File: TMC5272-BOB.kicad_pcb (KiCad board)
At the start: 2 copper layers, 103.1 x 51.1 mm, 23 parts, among them J1 Conn_02x14, J10 Conn_01x04_Socket, J11 Conn_01x04_Socket, J2 Conn_02x14, J22 Conn_01x01_Pin, J24 Conn_01x02_Socket, J26 Conn_01x01_Pin, J3 Conn_02x16, J4 Conn_02x12, J5 Conn_01x02_Pin, J6 Conn_01x03_Pin, J7 Conn_01x02_Pin, J8 Conn_01x02_Pin, J9 Conn_01x01_Pin

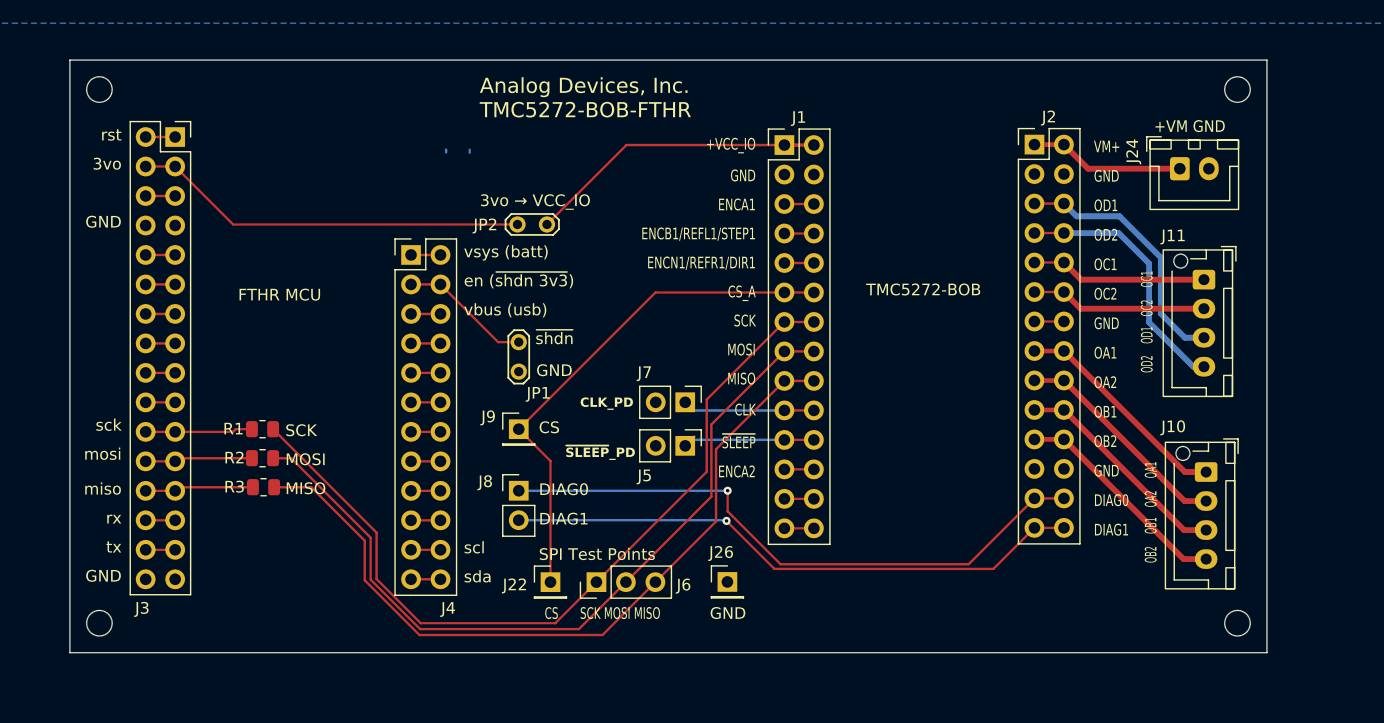
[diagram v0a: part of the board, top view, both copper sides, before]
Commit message: Fix BOB pin spacing.
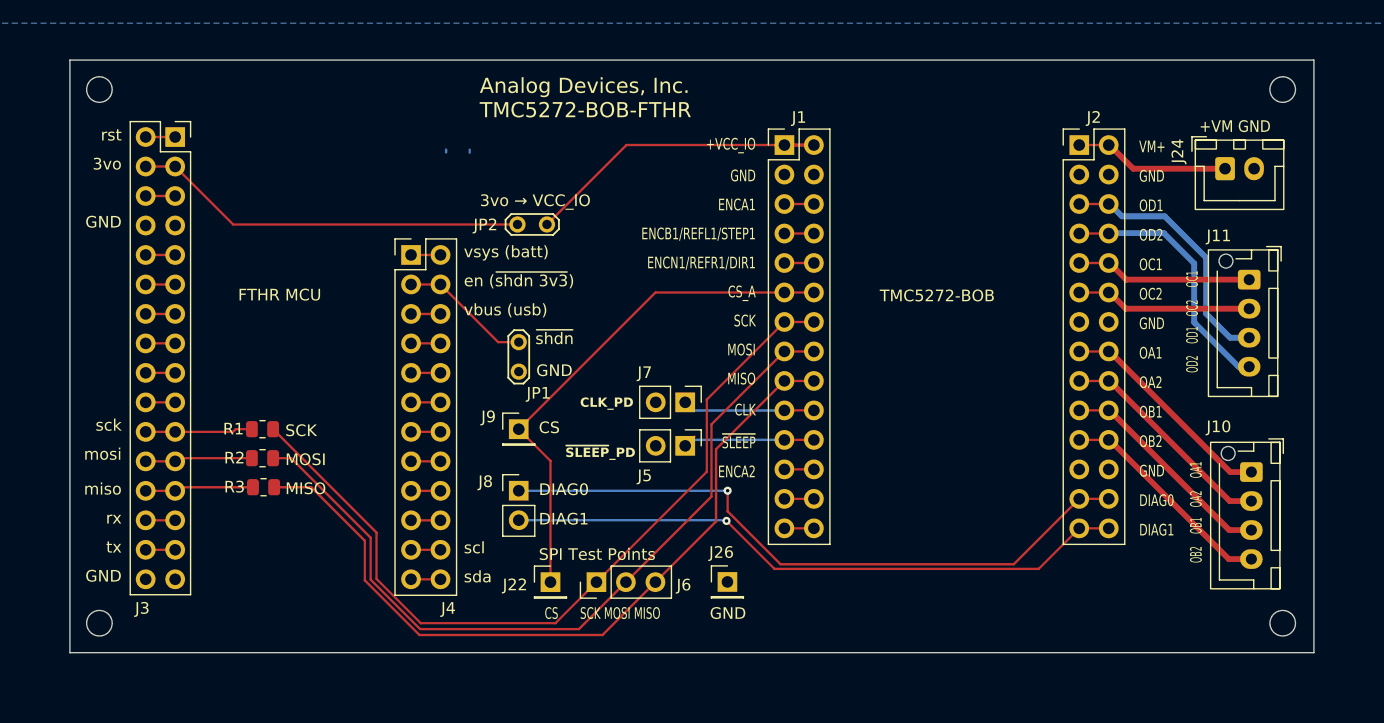
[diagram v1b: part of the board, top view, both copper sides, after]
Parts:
- moved J10 3.90 mm to (119.8, 48.2)
- moved J11 3.90 mm to (119.6, 31.6)
- moved J24 3.90 mm to (117.5, 22.1)
- moved REF** 3.90 mm to (122.5, 61.2)
- moved REF** 3.90 mm to (122.5, 15.2)
- moved J2 3.86 mm to (105.0, 20.0)
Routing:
- net DIAG1: track 50.2 -> 54.0 mm
- net DIAG0: track 53.0 -> 56.8 mm
- net GND: track 3.05 -> 0.51 mm
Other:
- board size 103.1 x 51.1 mm -> 107.2 x 51.1 mm
